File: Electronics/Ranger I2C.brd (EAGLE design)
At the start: 43.2 x 45.7 mm, 22 parts, among them IC1 ATmega328P, J1 PWR, J2 I2C, J3 FTDI, J4 AN, J5 5V, J6 GND, J7 PWR, J8 PWR, Q1 16MHz

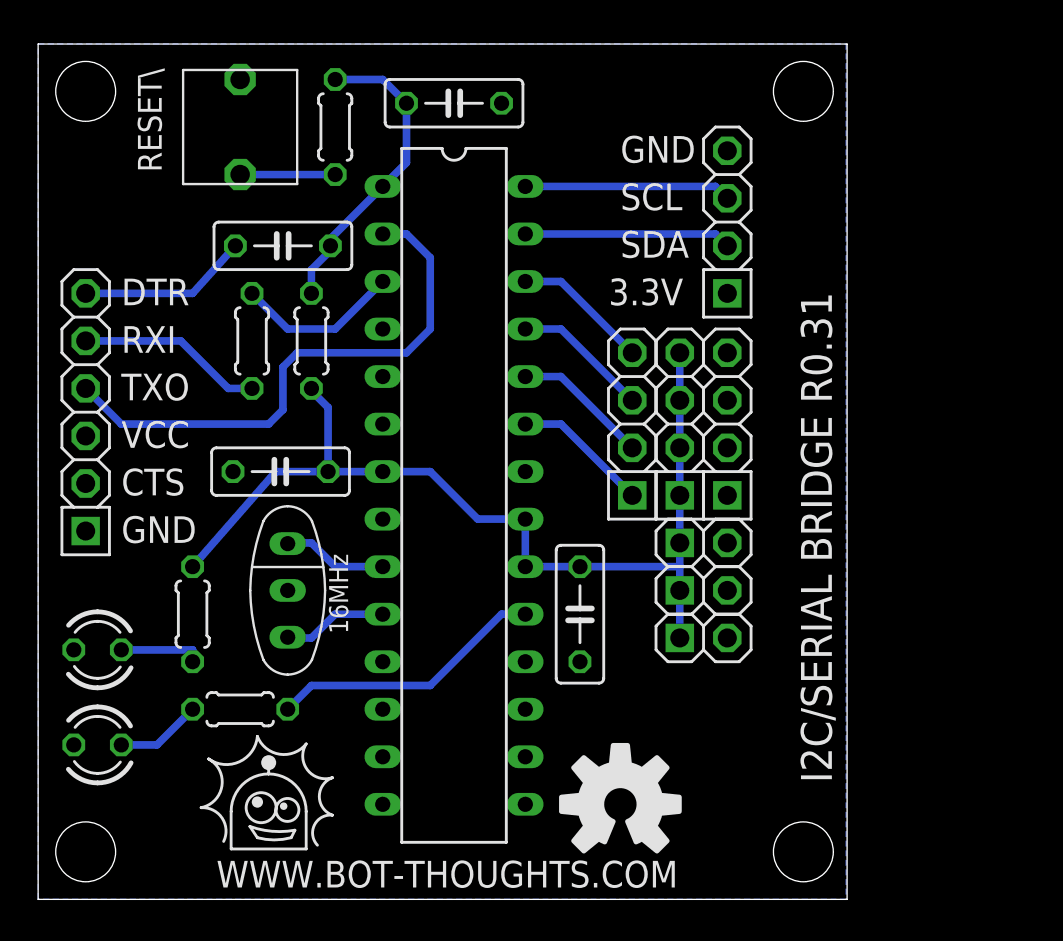
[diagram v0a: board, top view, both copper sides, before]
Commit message: Moved RC Mux to subdirectory. Minor changes to various other boards.
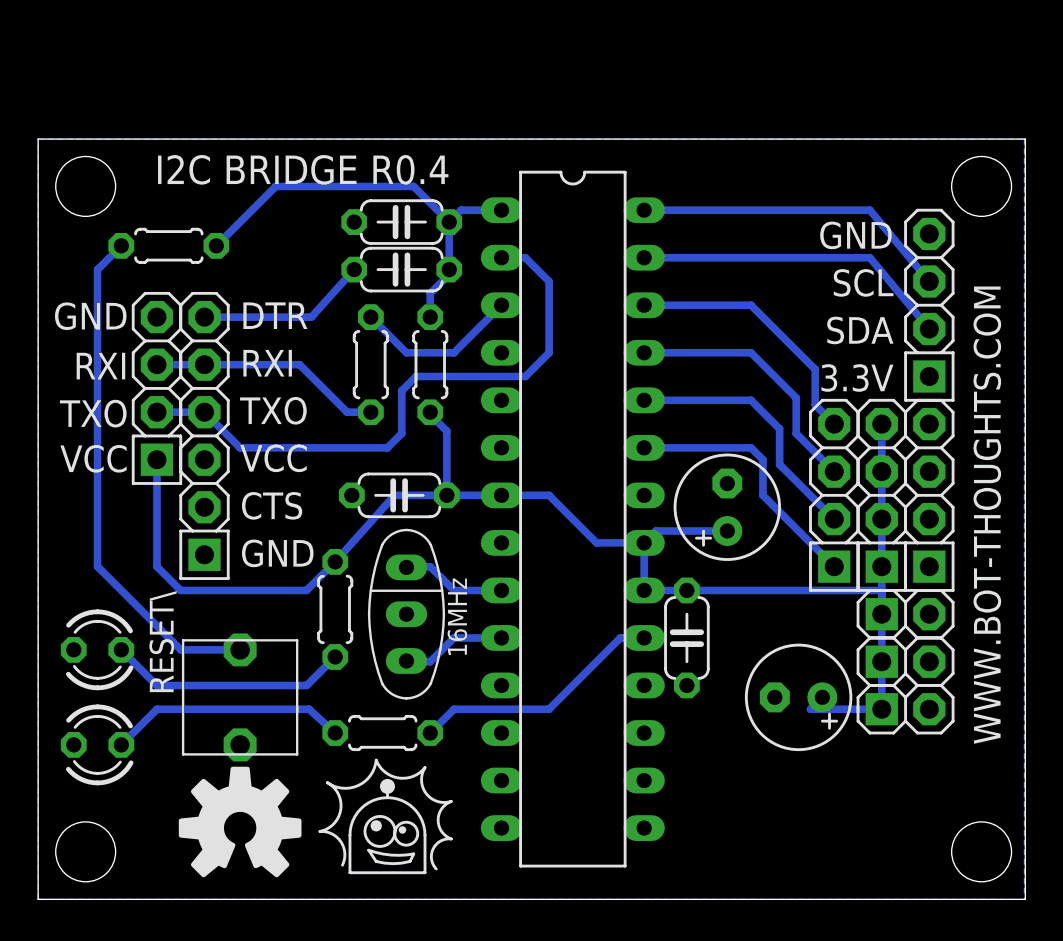
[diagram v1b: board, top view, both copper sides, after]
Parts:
- added C5: 470uF, rcl:E2,5-6
- added C6: 10uF, rcl:E2,5-6
- added J9: CAM, pinhead-2:1X04-S
- C1, C2, C3, C4: device rcl:C050-025X075 -> rcl:C050-024X044
- moved S1 35.6 mm to (10.8, 8.26), turned to 90 degrees
- moved J2 11.7 mm to (47.6, 31.8)
- moved J4 11.4 mm to (42.5, 21.6)
- moved J5 11.4 mm to (45.1, 21.6)
- moved J6 11.4 mm to (47.6, 21.6)
- moved J1 11.4 mm to (46.4, 15.2)
- moved J7 11.4 mm to (46.4, 12.7)
- moved J8 11.4 mm to (46.4, 10.2)
- moved R5 10.9 mm to (6.99, 34.9), turned to 180 degrees
- moved R2 7.73 mm to (18.4, 8.89)
- moved R7 7.62 mm to (15.9, 15.5)
- moved C2 6.94 mm to (19.4, 36.2), turned to 180 degrees
- moved R6 6.48 mm to (17.8, 28.6)
- moved J3 6.48 mm to (8.89, 24.8)
- moved C1 6.48 mm to (19.4, 33.7)
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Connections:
- net 5V: now also C5.+, C6.+, J9.1
- net <RXD/TXO: now also J9.2
- net GND: now also C5.-, C6.-, J9.4
- net LV_TXD/RXI>: now also J9.3
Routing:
- net 5V: track 52.0 -> 81.5 mm
- net N$7: track 5.08 -> 27.1 mm
- net N$8: track 4.45 -> 12.9 mm
- net N$4: track 4.60 -> 12.7 mm
- net ADC2: track 7.29 -> 13.9 mm
- net ADC0: track 7.29 -> 13.9 mm
- net ADC3: track 7.29 -> 13.9 mm
- net ADC1: track 7.29 -> 13.9 mm
- net N$6: track 16.6 -> 23.1 mm
- net SDA: track 11.1 -> 17.0 mm
- net SCL: track 11.1 -> 17.0 mm
- net LV_TXD/RXI>: track 9.94 -> 12.5 mm
- net <RXD/TXO: track 29.5 -> 32.1 mm
- net N$5: track 14.8 -> 13.5 mm
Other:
- board size 43.2 x 45.7 mm -> 52.8 x 40.6 mm
- board text added: "I2C BRIDGE R0.4"
- board text removed: "I2C/SERIAL BRIDGE R0.31"
